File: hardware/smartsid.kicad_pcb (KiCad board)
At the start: 2 copper layers, 50.8 x 57.8 mm, 63 parts, among them P1 INPUT, P2 CONTROL, P4 SOCKET LEFT, P5 OUTPUT, P6 SOCKET RIGHT, Q1 BC547, Q2 BC547, U1 GAL16V8, U2 SID2, U3 7812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

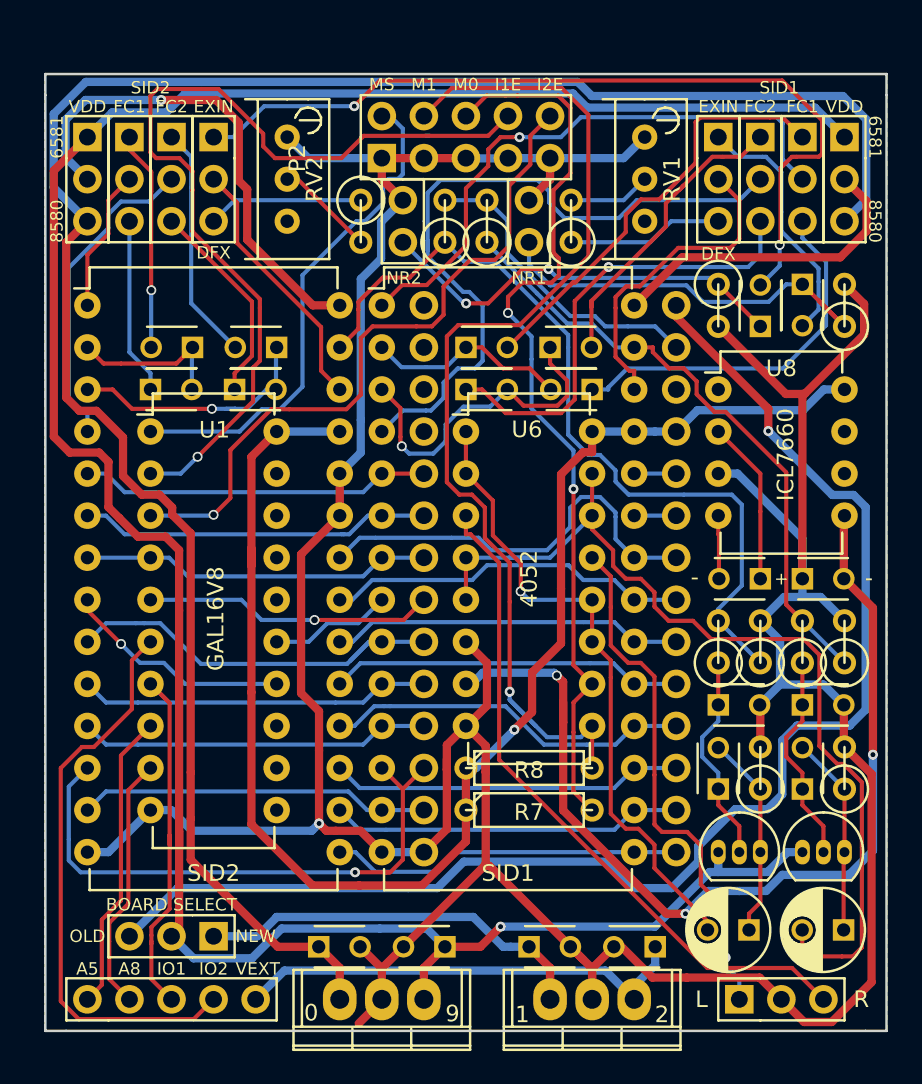
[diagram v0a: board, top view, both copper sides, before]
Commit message: Hardware: Improved routing and silkscreen
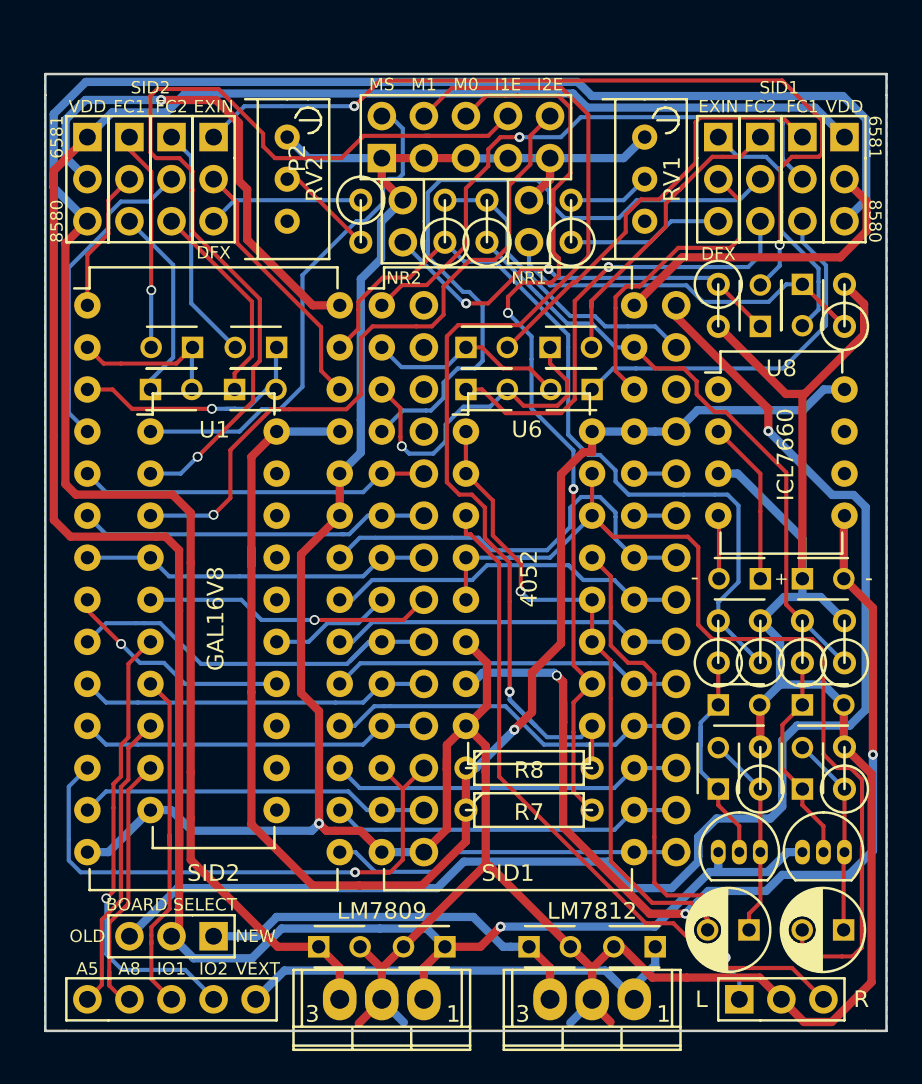
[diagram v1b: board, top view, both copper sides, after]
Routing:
- net /RIGHT: track 58.6 -> 69.8 mm
- net /~IO2: track 34.5 -> 27.6 mm, vias 0 -> 1
- net GND: track 240.8 -> 246.5 mm
- net /+9V: track 121.9 -> 124.1 mm
- net /LEFT: track 38.8 -> 40.3 mm
- net Net-(C15-Pad1): track 12.8 -> 14.2 mm
- net VDD: track 83.8 -> 85.2 mm
- net /+12V: track 151.2 -> 152.5 mm
- net /A8: track 15.5 -> 16.7 mm
- net Net-(C4-Pad1): track 10.7 -> 11.8 mm
- net /VEE: track 59.2 -> 59.8 mm
- net /RIGHT_OUT: track 41.3 -> 41.9 mm
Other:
- board text added: "3"
- board text added: "LM7809"
- board text added: "LM7812"
- board text removed: "0"
- board text removed: "2"
- board text removed: "9"

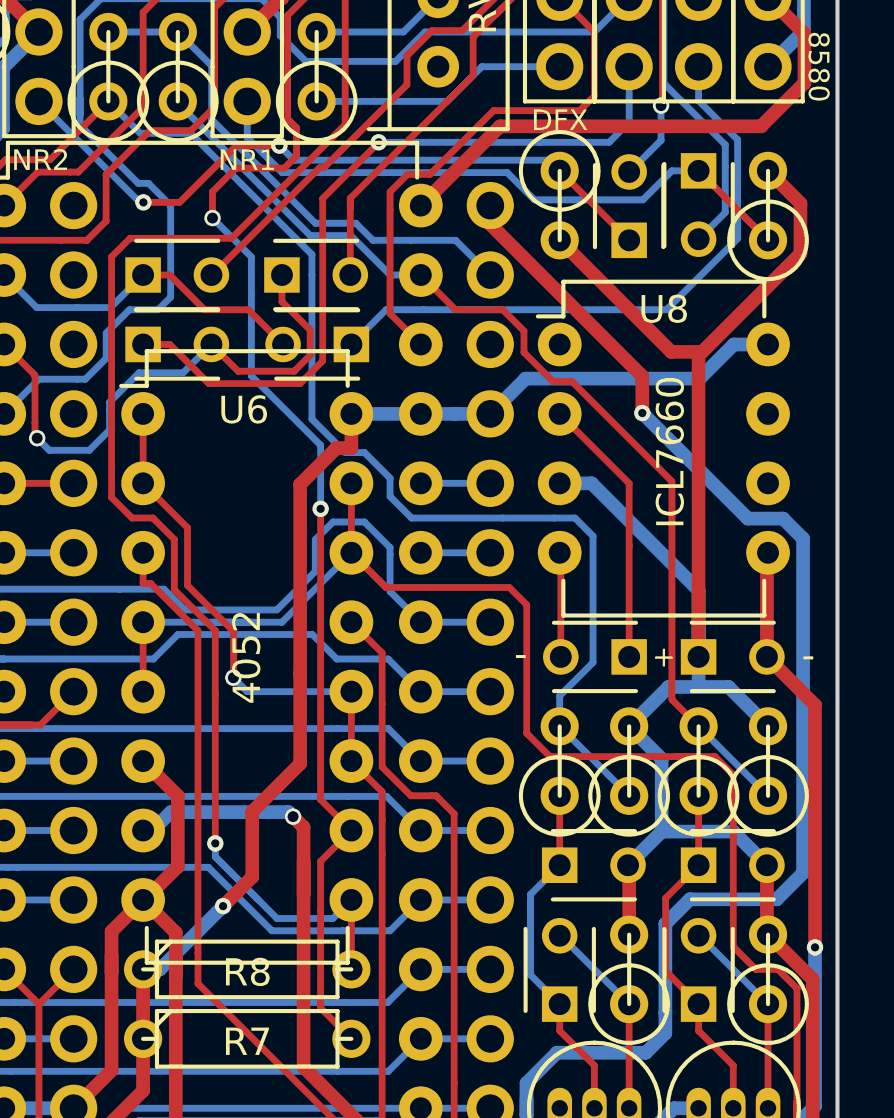
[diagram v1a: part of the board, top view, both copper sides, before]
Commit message: Hardware: Flipped VEE bypass cap allowing less ambigious silkscreen
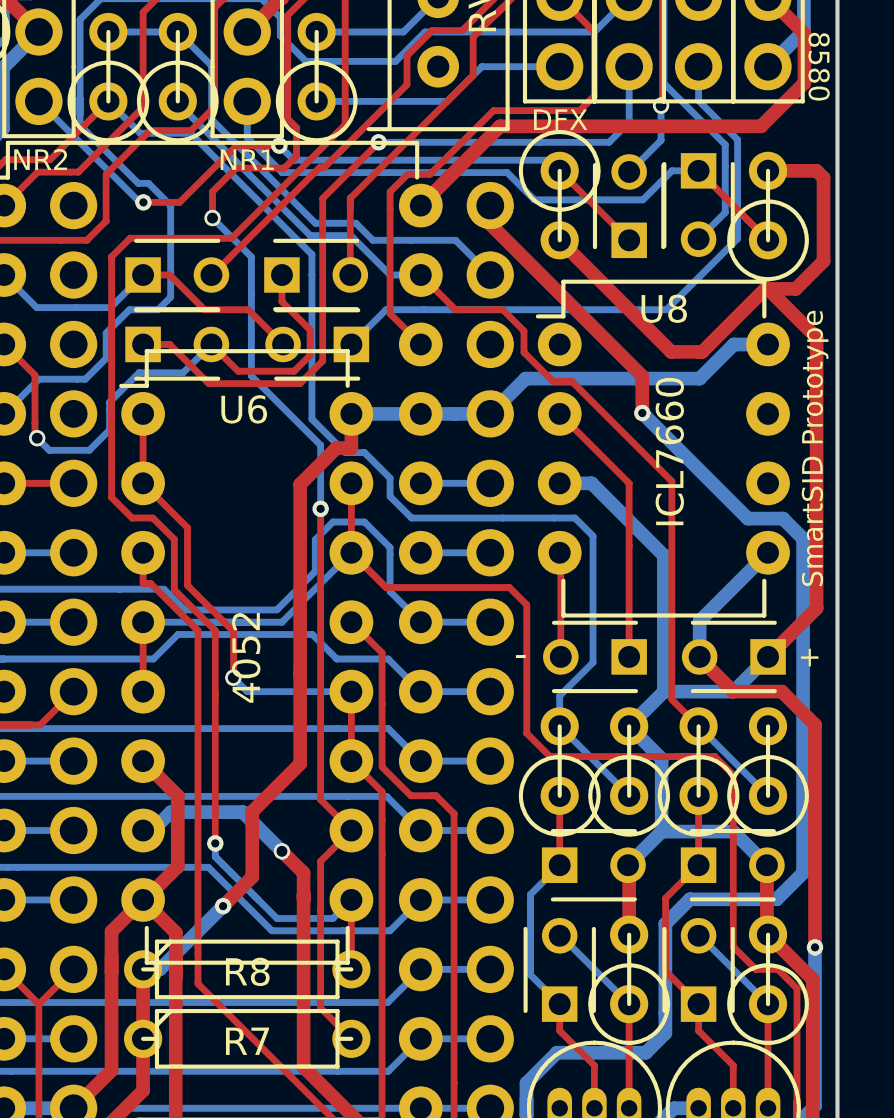
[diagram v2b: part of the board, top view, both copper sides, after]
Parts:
- moved C18 2.54 mm to (176.5, 97.8), turned to 180 degrees
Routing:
- net GND: track 246.5 -> 251.4 mm
- net /VEE: track 59.8 -> 61.1 mm
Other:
- board text added: "SmartSID Prototype"

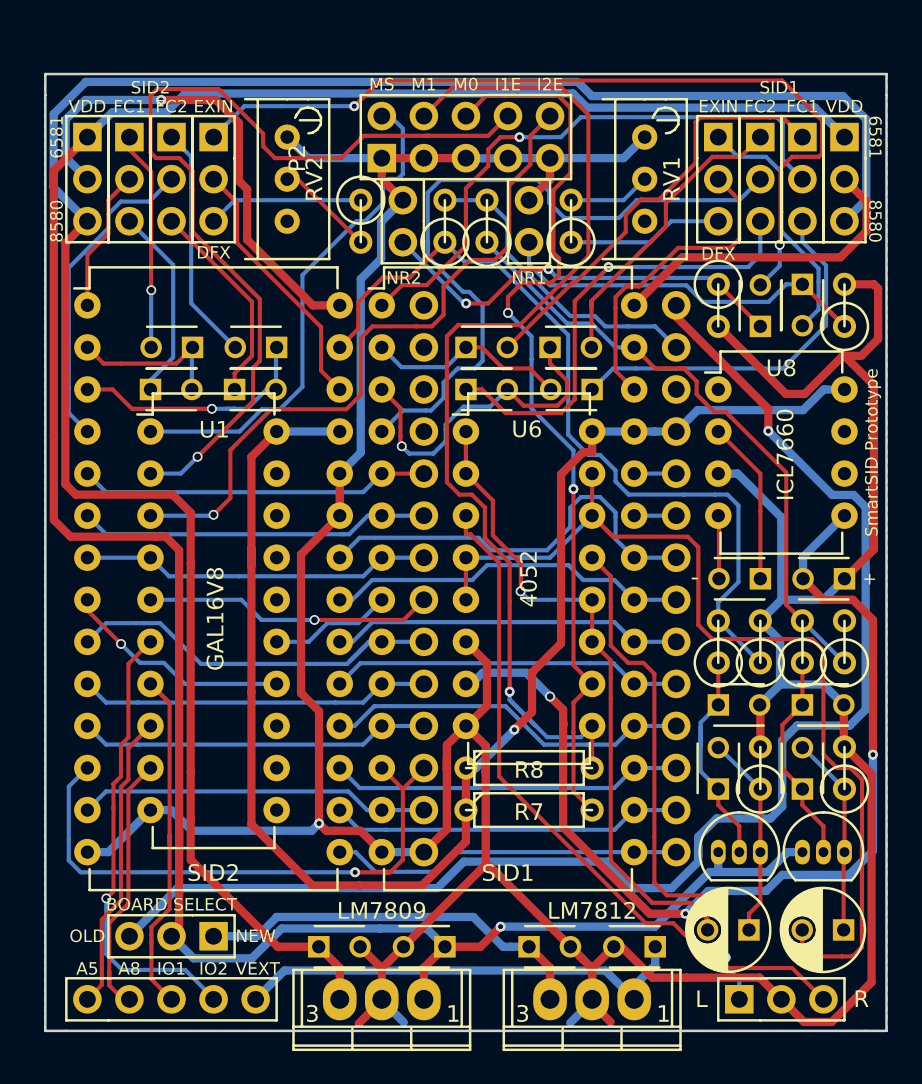
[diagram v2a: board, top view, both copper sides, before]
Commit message: Hardware: Rearranged components to increase top clearance, rerouted
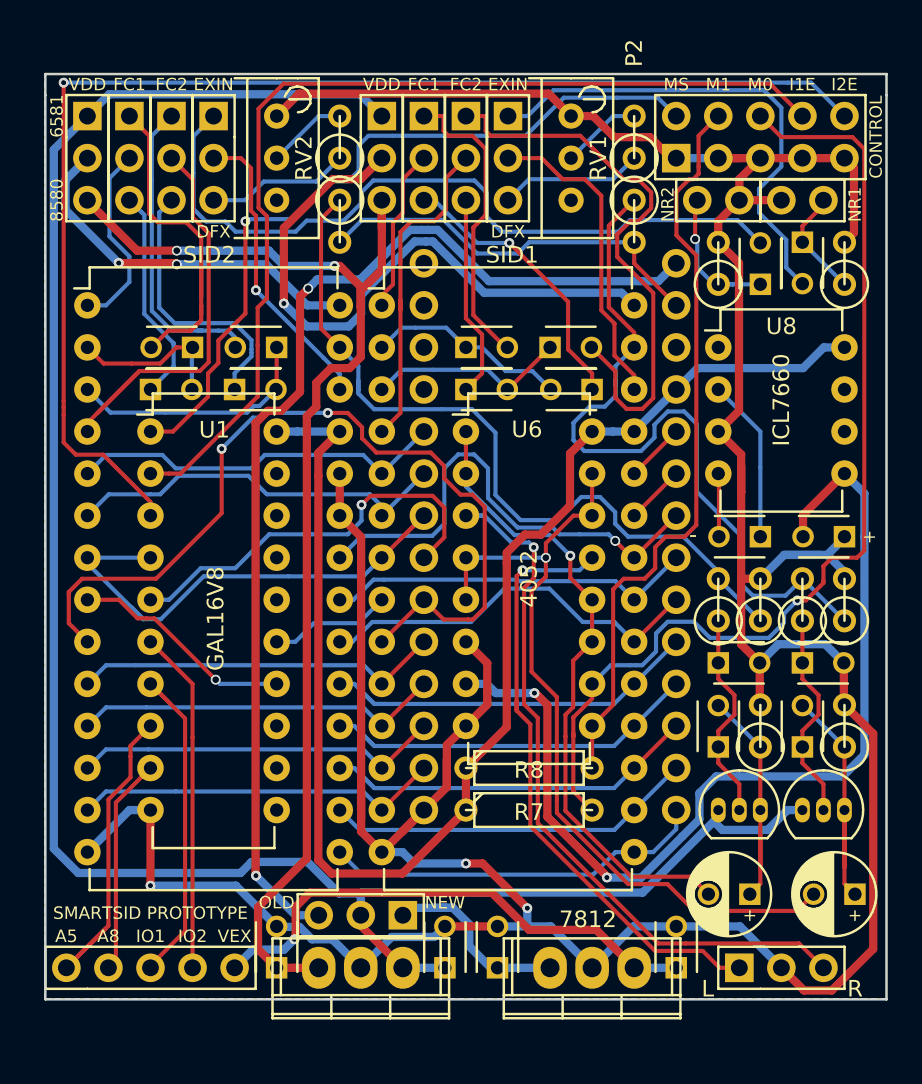
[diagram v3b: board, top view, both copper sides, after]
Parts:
- moved JP5 28.0 mm to (148.6, 69.8)
- moved JP7 22.9 mm to (151.1, 69.8)
- moved JP9 18.0 mm to (175.3, 74.9), turned to 270 degrees
- moved JP10 18.0 mm to (167.6, 74.9), turned to 90 degrees
- moved JP6 17.8 mm to (153.7, 69.8)
- moved P2 17.8 mm to (166.4, 72.4)
- moved JP11 12.8 mm to (156.2, 69.8)
- moved JP4 11.5 mm to (149.9, 118.1)
- moved R14 8.89 mm to (163.8, 76.2), turned to 270 degrees
- moved R10 6.35 mm to (163.8, 71.1)
- moved R13 6.35 mm to (146.1, 76.2), turned to 270 degrees
- moved R1 5.24 mm to (146.1, 71.1), turned to 90 degrees
- moved RV1 4.62 mm to (160.0, 69.8)
- moved C8 2.84 mm to (142.2, 121.3), turned to 90 degrees
- moved C14 2.54 mm to (174.0, 77.5)
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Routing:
- net /+9V: track 124.1 -> 75.0 mm, vias 0 -> 2
- net /~IO2EN: track 42.0 -> 77.3 mm
- net /+12V: track 152.5 -> 122.2 mm, vias 1 -> 0
- net /A0: track 24.8 -> 53.4 mm, vias 0 -> 2
- net Net-(JP7-Pad2): track 35.6 -> 10.2 mm, vias 1 -> 0
- net Net-(JP6-Pad2): track 43.5 -> 20.0 mm
- net /M1: track 65.3 -> 45.1 mm, vias 1 -> 0
- net /RIGHT: track 69.8 -> 50.2 mm, vias 0 -> 1
- net /PWR1: track 19.6 -> 38.3 mm, vias 0 -> 1
- net Net-(C14-Pad1): track 25.0 -> 6.66 mm
- net VDD: track 85.2 -> 67.5 mm, vias 1 -> 2
- net Net-(C13-Pad1): track 25.4 -> 9.47 mm, vias 2 -> 1
- net Net-(C9-Pad2): track 18.6 -> 34.5 mm
- net Net-(C10-Pad1): track 27.8 -> 12.2 mm, vias 1 -> 0
- net /MS: track 31.0 -> 46.3 mm, vias 0 -> 1
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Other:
- board size 50.8 x 57.8 mm -> 50.8 x 55.9 mm
- board text added: "7812"
- board text added: "CONTROL"
- board text added: "SMARTSID PROTOTYPE"
- board text added: "VEX"
- board text removed: "1"
- board text removed: "3"
- board text removed: "BOARD SELECT"
- board text removed: "LM7809"
- board text removed: "LM7812"
- board text removed: "SID1"
- board text removed: "SID2"
- board text removed: "SmartSID Prototype"
- board text removed: "VEXT"

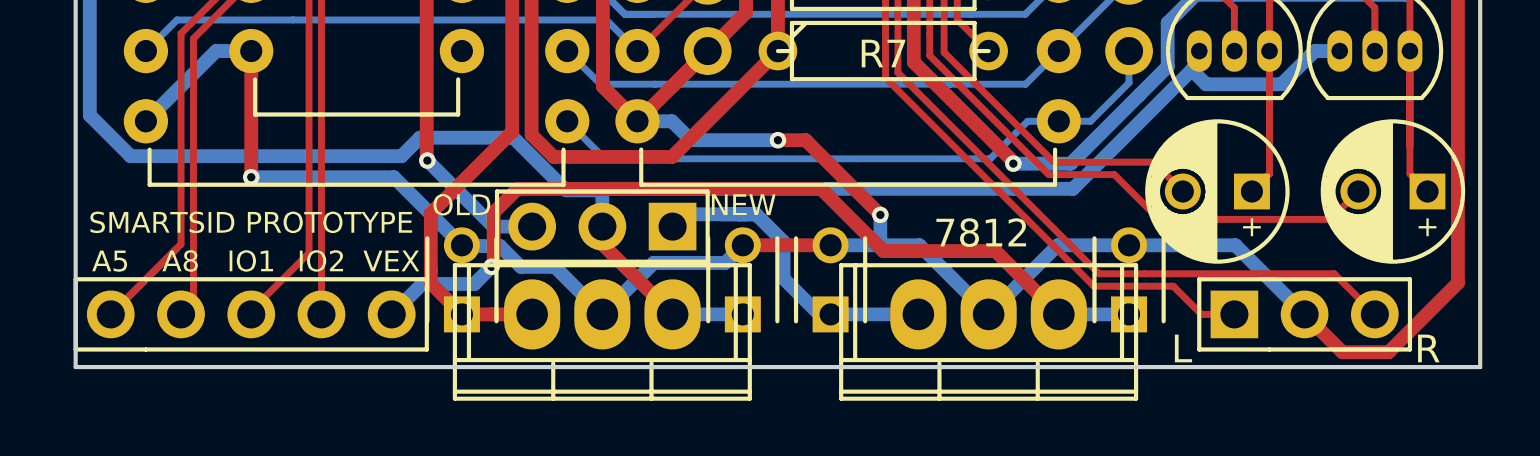
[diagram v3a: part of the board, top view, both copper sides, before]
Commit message: Hardware: Improved routing and silkscreen
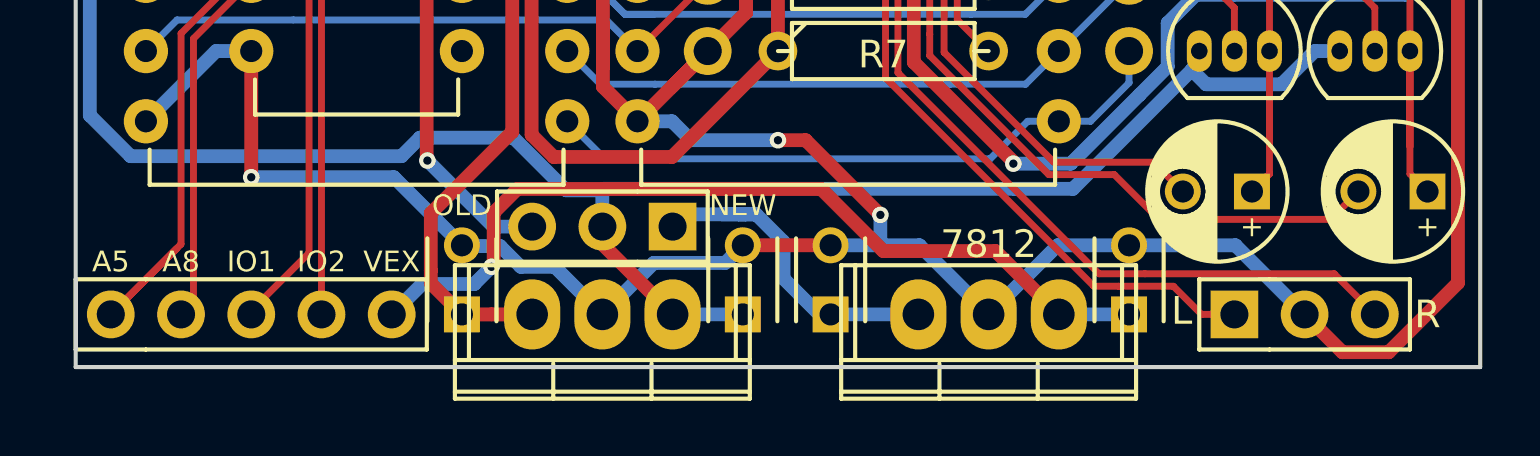
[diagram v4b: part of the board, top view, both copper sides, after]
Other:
- board text removed: "SMARTSID PROTOTYPE"
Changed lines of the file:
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@@
     (area 128.194999 67.234999 179.145001 123.265001)
     (thickness 1.6)
-    (drawings 43)
+    (drawings 42)
     (tracks 995)
     (zones 0)
@@
   (gr_line (start 128.27 123.19) (end 179.07 123.19) (angle 90) (layer Edge.Cuts) (width 0.15))
   (gr_line (start 128.27 68.58) (end 128.27 123.19) (angle 90) (layer Edge.Cuts) (width 0.15))
-  (gr_text 7812 (at 161.036 118.364) (layer F.SilkS)
+  (gr_text 7812 (at 161.29 118.745) (layer F.SilkS)
     (effects (font (size 1 1) (thickness 0.15)))
   )
-  (gr_text "SMARTSID PROTOTYPE" (at 134.62 117.983) (layer F.SilkS)
-    (effects (font (size 0.75 0.75) (thickness 0.15)))
-  )
   (gr_text + (at 178.054 95.25) (layer F.SilkS)
     (effects (font (size 0.75 0.75) (thickness 0.15)))
@@
     (effects (font (size 0.75 0.75) (thickness 0.15)))
   )
-  (gr_text R (at 177.165 122.555) (layer F.SilkS)
+  (gr_text R (at 177.165 121.285) (layer F.SilkS)
     (effects (font (size 1 1) (thickness 0.15)))
   )
-  (gr_text L (at 168.275 122.555) (layer F.SilkS)
+  (gr_text L (at 168.275 121.158) (layer F.SilkS)
     (effects (font (size 1 1) (thickness 0.15)))
   )
